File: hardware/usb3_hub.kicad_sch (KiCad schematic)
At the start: 39 parts, among them J7 USB3_B, J9 USB3_A, U8 USB7206C-I/KDX

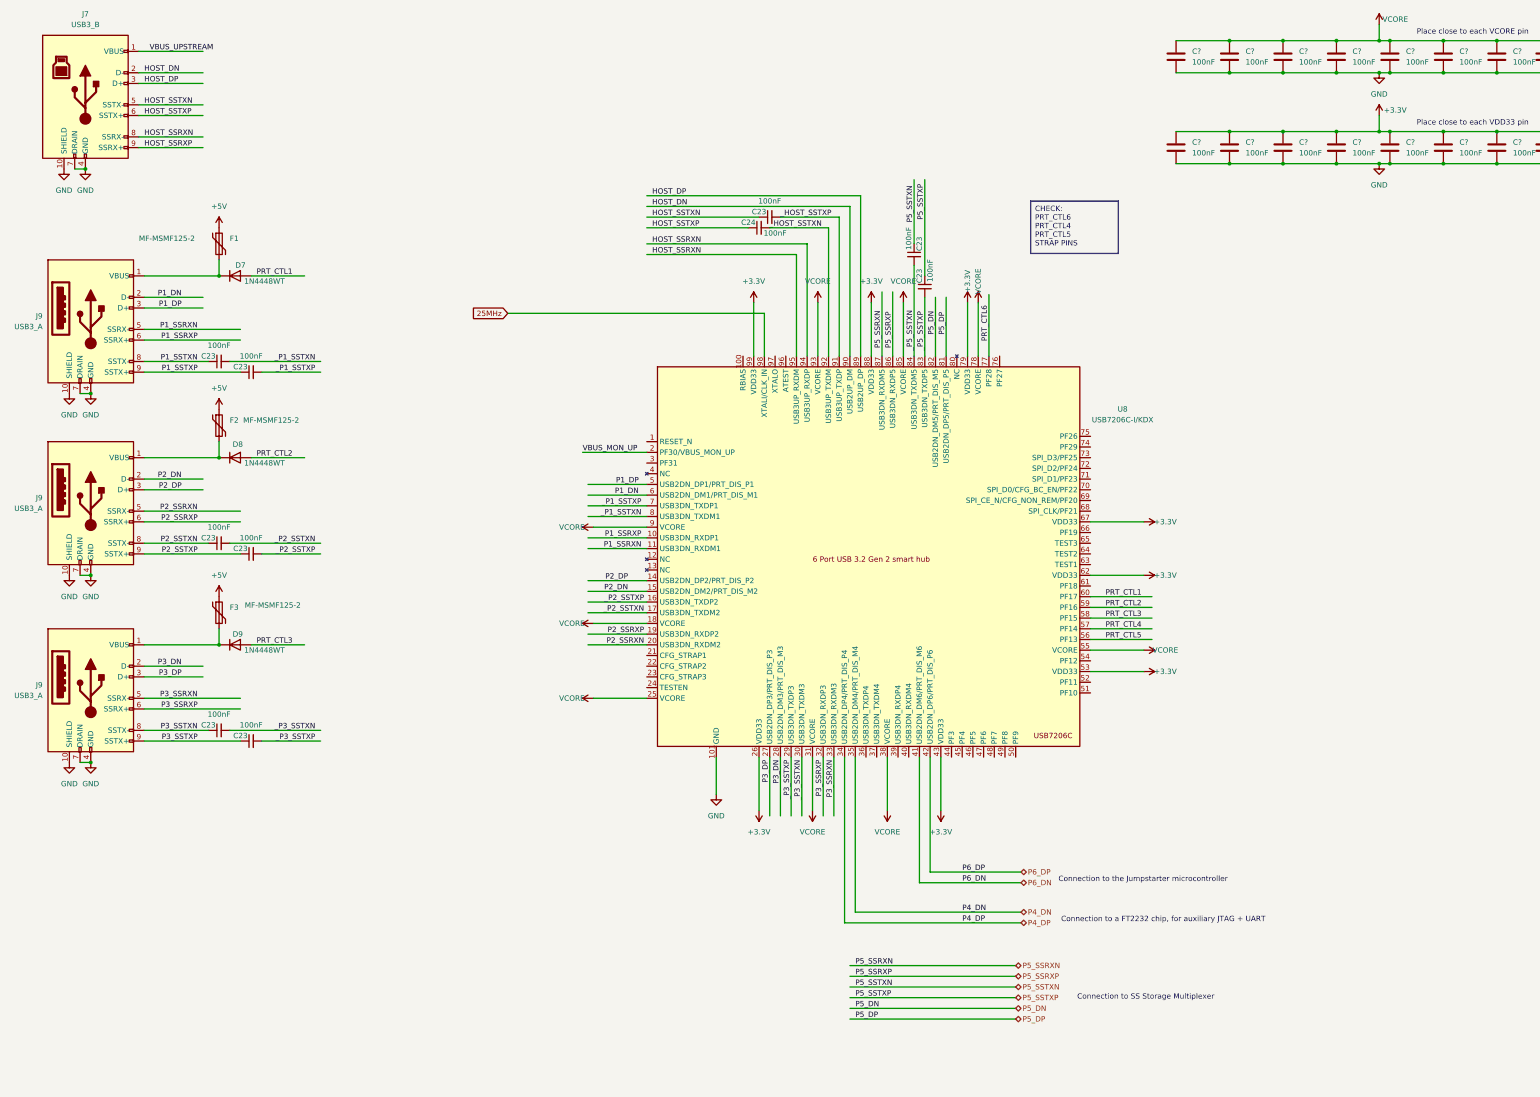
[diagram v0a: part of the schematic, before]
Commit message: Started routing USB3 diff pairs
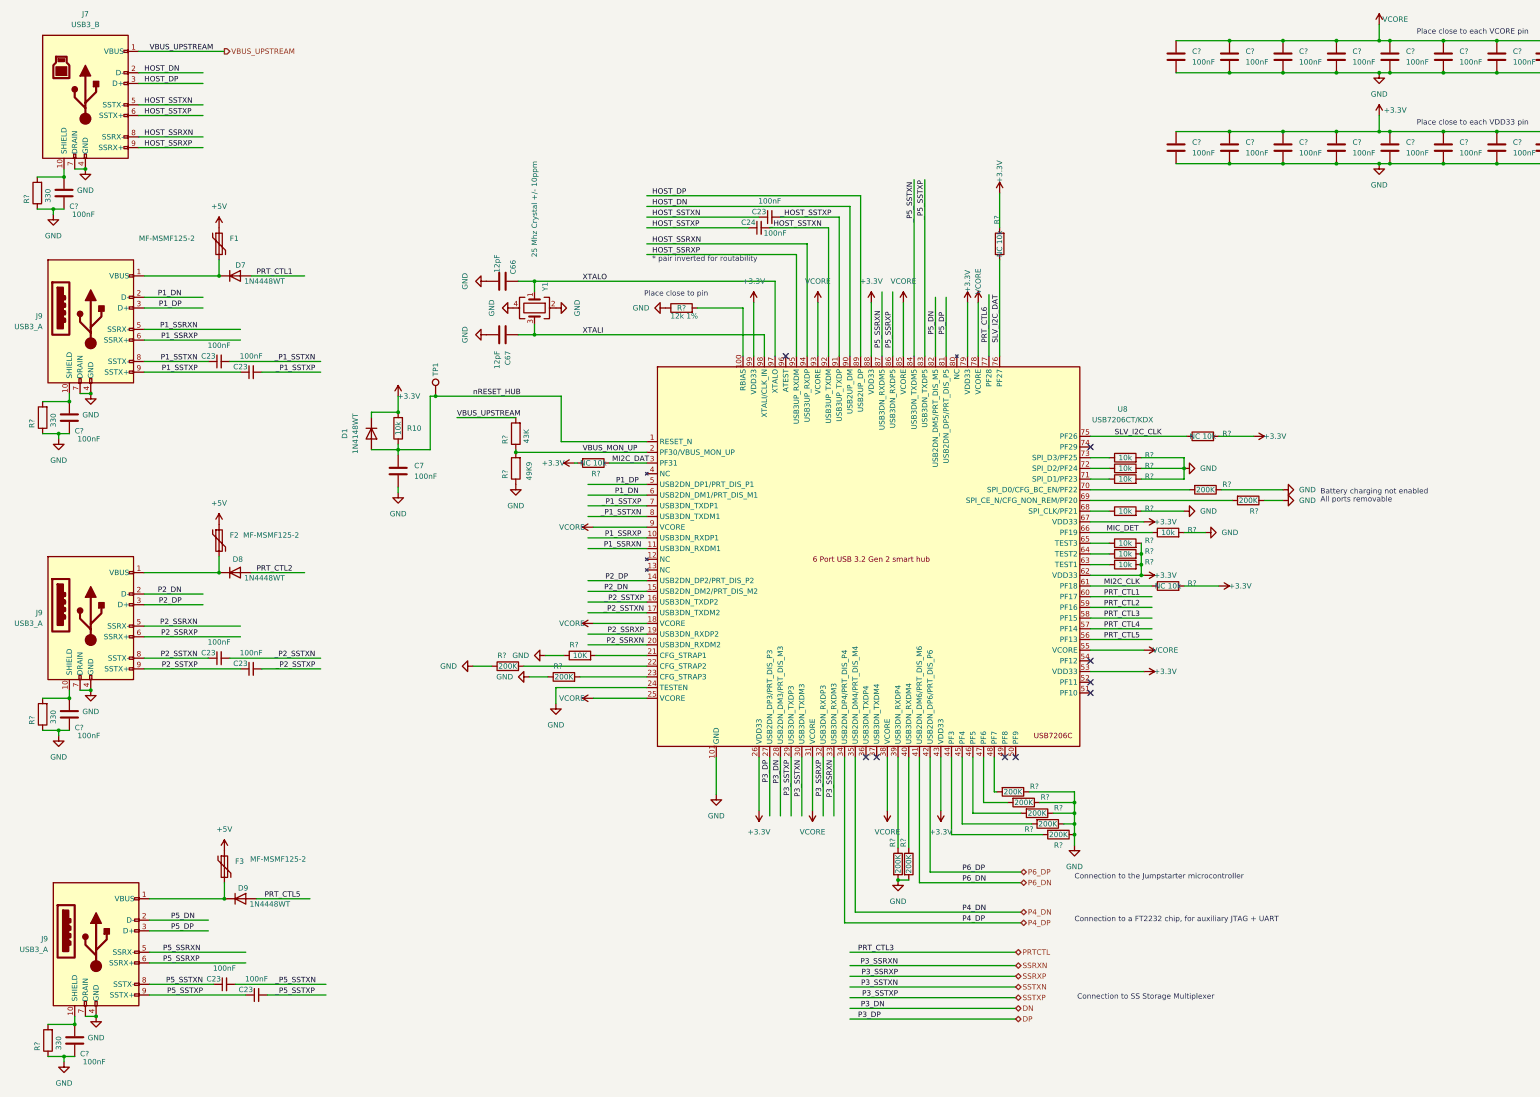
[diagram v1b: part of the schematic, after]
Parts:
- removed C23 (x2): 100nF, Capacitor_SMD:C_0402_1005Metric, symbol Device:C_Small
- added C66, C67: 12pF, Capacitor_SMD:C_0402_1005Metric, symbol Device:C
- added C7, C? (x4): 100nF, Capacitor_SMD:C_0402_1005Metric, symbol Device:C
- added D1: 1N4148WT, Diode_SMD:D_SOD-523, symbol Diode:1N4148WT
- added R10, R? (x8): 10k, Resistor_SMD:R_0402_1005Metric, symbol Device:R
- added R? (x11): 200K, Resistor_SMD:R_0402_1005Metric, symbol Device:R
- added R?: 49K9, Resistor_SMD:R_0402_1005Metric, symbol Device:R
- added R? (x4): 330, Resistor_SMD:R_0402_1005Metric, symbol Device:R
- added R? (x4): NC 10k, Resistor_SMD:R_0402_1005Metric, symbol Device:R
- added R?: 43K, Resistor_SMD:R_0402_1005Metric, symbol Device:R
- added R?: 12k 1%, Resistor_SMD:R_0402_1005Metric, symbol Device:R
- added R?: 10K, Resistor_SMD:R_0402_1005Metric, symbol Device:R
- added TP1: TestPoint, TestPoint:TestPoint_Pad_D1.0mm, symbol Connector:TestPoint
- added Y1: 25 Mhz Crystal +/- 10ppm, Oscillator:Oscillator_SMD_EuroQuartz_XO32-4Pin_3.2x2.5mm, symbol Device:Crystal_GND24
- C23, C24, C? (x18): MPN (none) -> CL05B104K05NNNC; MPN2 (none) -> TCC0402X7R104M160AT
- D7: MPN (none) -> 1N4448WT
- J9: footprint Connector_USB:USB3_A_Molex_48393-001 -> Connector_USB:SS-52000-004
- J9: footprint Connector_USB:USB3_A_Molex_48393-001 -> Connector_USB:SS-52000-004; Link (none) -> https://eu.mouser.com/ProductDetail/Stewart-Connector-Bel/S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; MFR Part (none) -> SS-52000-004
- U8: value USB7206C-I/KDX -> USB7206CT/KDX; Link (none) -> https://www.mouser.es/ProductDetail/Microchip-Technology/US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; MPN (none) -> USB7206CT/KDX
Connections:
- net P3_SSTXN is gone; now on net P5_SSTXN: C23.1, J9.8 (SSTX-)
- net P3_SSTXP is gone; now on net P5_SSTXP: C23.1, J9.9 (SSTX+)
- net +3.3V: now also D1.1 (K), R10.2, R?.2, R?.2, R?.2, R?.2, R?.2, R?.2, R?.2
- net GND: now also U8.24 (TESTEN), C66.1, C67.1, C7.1, C?.2, C?.2, C?.2, C?.2, R?.1, R?.1, R?.1, R?.1, R?.1, R?.1, R?.1, R?.1, R?.1, R?.1, R?.1, R?.1, R?.1, R?.1, R?.1, R?.1, R?.2, R?.2, R?.2, R?.2, R?.2, R?.2, R?.2, Y1.2, Y1.4; no longer J7.10 (SHIELD), J9.10 (SHIELD), J9.10 (SHIELD), J9.10 (SHIELD)
- net HOST_SSRXN: no longer U8.95 (USB3UP_RXDM)
- net HOST_SSRXP: now also U8.95 (USB3UP_RXDM)
- net P5_DN: now also J9.2 (D-)
- net P5_DP: now also J9.3 (D+)
- net P5_SSRXN: now also J9.5 (SSRX-)
- net P5_SSRXP: now also J9.6 (SSRX+)
- net PRT_CTL5: now also D9.2 (A)
- net VBUS_MON_UP: now also R?.1, R?.2
- net VBUS_UPSTREAM: now also R?.2
- net _P5_SSTXN: now also C23.2
- net _P5_SSTXP: now also C23.2
- net nRESET_HUB: now reaches U8.1 (RESET_N)
- net nRESET_HUB: now also C7.2, D1.2 (A), R10.1, TP1.1
- net at U8.100 (RBIAS): now also R?.2
- net at U8.21 (CFG_STRAP1): now also R?.2
- net at U8.22 (CFG_STRAP2): now also R?.2
- net at U8.23 (CFG_STRAP3): now also R?.2
- net MI2C_DAT: now reaches U8.3 (PF31)
- net MI2C_DAT: now also R?.1
- net at U8.39 (USB3DN_RXDP4): now also R?.1
- net at U8.40 (USB3DN_RXDM4): now also R?.1
- net at U8.44 (PF3): now also R?.2
- net at U8.45 (PF4): now also R?.2
- net at U8.46 (PF5): now also R?.2
- net at U8.47 (PF6): now also R?.2
- net at U8.48 (PF7): now also R?.2
- net MI2C_CLK: now reaches U8.61 (PF18)
- net MI2C_CLK: now also R?.1
- net at U8.63 (TEST1): now also R?.1
- net at U8.64 (TEST2): now also R?.1
- net at U8.65 (TEST3): now also R?.1
- net MIC_DET: now reaches U8.66 (PF19)
- net MIC_DET: now also R?.1
- net at U8.68 (SPI_CLK/PF21): now also R?.1
- net at U8.69 (SPI_CE_N/CFG_NON_REM/PF20): now also R?.2
- net at U8.70 (SPI_D0/CFG_BC_EN/PF22): now also R?.2
- net at U8.71 (SPI_D1/PF23): now also R?.1
- net at U8.72 (SPI_D2/PF24): now also R?.1
- net at U8.73 (SPI_D3/PF25): now also R?.1
- net SLV_I2C_CLK: now reaches U8.75 (PF26)
- net SLV_I2C_CLK: now also R?.1
- net SLV_I2C_DAT: now reaches U8.76 (PF27)
- net SLV_I2C_DAT: now also R?.1
- net XTALO: now reaches U8.97 (XTALO)
- net XTALO: now also C66.2, Y1.1
- net 25MHz renamed XTALI
- net XTALI: now also C67.2, Y1.3
- net P3_DN renamed DN
- net DN: no longer J9.2 (D-)
- net P3_DP renamed DP
- net DP: no longer J9.3 (D+)
- net P3_SSRXN renamed SSRXN
- net SSRXN: no longer J9.5 (SSRX-)
- net P3_SSRXP renamed SSRXP
- net SSRXP: no longer J9.6 (SSRX+)
- net PRT_CTL3 renamed PRTCTL
- net PRTCTL: no longer D9.2 (A)
- net _P3_SSTXN renamed SSTXN
- net SSTXN: no longer C23.2
- net _P3_SSTXP renamed SSTXP
- net SSTXP: no longer C23.2
- new net: C?.1, J9.10 (SHIELD), R?.2 (x3)
- new net: C?.1, J7.10 (SHIELD), R?.2
- no-connect marks 0 -> 9
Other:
- note added: "* pair inverted for routability"
- note added: "All ports removable"
- note added: "Battery charging not enabled"
- note added: "Place close to pin"
- moved on the sheet: C23, D8, D9, F2, F3, J9

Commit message: Routing and several design fixes
Signed-off-by: Miguel Angel Ajo Pelayo <majopela@redhat.com>
Signed-off-by: Ricardo Noriega <rnoriega@redhat.com>
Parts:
- R? (x3): value NC 10k -> 10k; fit_field dnp -> (none)
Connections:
- net +3.3V: no longer R?.2, R?.2, R?.2
- net GND: now also R?.2, R?.2, R?.2
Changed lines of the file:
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@@
     )
   )
-  (symbol (lib_id "power:+3.3V") (at 307.975 116.84 270) (unit 1)
-    (in_bom yes) (on_board yes) (dnp no)
-    (property "Reference" "#PWR013" (at 304.165 116.84 0)
+  (symbol (lib_id "power:GND") (at 307.975 116.84 90) (unit 1)
+    (in_bom yes) (on_board yes) (dnp no) (fields_autoplaced)
+    (property "Reference" "#PWR?" (at 314.325 116.84 0)
       (effects (font (size 1.27 1.27)) hide)
     )
-    (property "Value" "+3.3V" (at 313.055 116.84 90)
-      (effects (font (size 1.27 1.27)))
+    (property "Value" "GND" (at 311.785 116.84 90)
+      (effects (font (size 1.27 1.27)) (justify right))
     )
     (property "Footprint" "" (at 307.975 116.84 0)
@@
       (project "jumpstarter"
         (path "/5e49fb74-0a9b-4946-8b59-2b8244d10fd9"
-          (reference "#PWR013") (unit 1)
+          (reference "#PWR?") (unit 1)
+        )
+        (path "/5e49fb74-0a9b-4946-8b59-2b8244d10fd9/0a246f5a-dd08-4f47-947a-3b89ae06d789"
+          (reference "#PWR03") (unit 1)
         )
         (path "/5e49fb74-0a9b-4946-8b59-2b8244d10fd9/c1addf8b-26b2-43fb-875c-11d76afd1403"
@@
       (effects (font (size 1.27 1.27)))
     )
-    (property "Value" "NC 10k" (at 287.655 152.4 90)
+    (property "Value" "10k" (at 287.655 152.4 90)
       (effects (font (size 1.27 1.27)))
     )
@@
       (effects (font (size 1.27 1.27)) hide)
     )
-    (property "fit_field" "dnp" (at 287.655 152.4 90)
-      (effects (font (size 1.27 1.27)) hide)
-    )
     (pin "1")
     (pin "2")
@@
     )
   )
+  (symbol (lib_id "power:GND") (at 299.72 152.4 90) (unit 1)
+    (in_bom yes) (on_board yes) (dnp no) (fields_autoplaced)
+    (property "Reference" "#PWR?" (at 306.07 152.4 0)
+      (effects (font (size 1.27 1.27)) hide)
+    )
+    (property "Value" "GND" (at 303.53 152.4 90)
+      (effects (font (size 1.27 1.27)) (justify right))
+    )
+    (property "Footprint" "" (at 299.72 152.4 0)
+      (effects (font (size 1.27 1.27)) hide)
+    )
+    (property "Datasheet" "" (at 299.72 152.4 0)
+      (effects (font (size 1.27 1.27)) hide)
+    )
+    (pin "1")
+    (instances
+      (project "jumpstarter"
+        (path "/5e49fb74-0a9b-4946-8b59-2b8244d10fd9"
+          (reference "#PWR?") (unit 1)
+        )
+        (path "/5e49fb74-0a9b-4946-8b59-2b8244d10fd9/0a246f5a-dd08-4f47-947a-3b89ae06d789"
+          (reference "#PWR03") (unit 1)
+        )
+        (path "/5e49fb74-0a9b-4946-8b59-2b8244d10fd9/c1addf8b-26b2-43fb-875c-11d76afd1403"
+          (reference "#PWR083") (unit 1)
+        )
+      )
+    )
+  )
   (symbol (lib_id "power:+3.3V") (at 190.5 205.74 180) (unit 1)
     (in_bom yes) (on_board yes) (dnp no)
@@
     )
   )
-  (symbol (lib_id "power:+3.3V") (at 247.65 59.055 0) (unit 1)
-    (in_bom yes) (on_board yes) (dnp no)
-    (property "Reference" "#PWR013" (at 247.65 62.865 0)
-      (effects (font (size 1.27 1.27)) hide)
-    )
-    (property "Value" "+3.3V" (at 247.65 53.975 90)
-      (effects (font (size 1.27 1.27)))
-    )
-    (property "Footprint" "" (at 247.65 59.055 0)
-      (effects (font (size 1.27 1.27)) hide)
-    )
-    (property "Datasheet" "" (at 247.65 59.055 0)
-      (effects (font (size 1.27 1.27)) hide)
-    )
-    (pin "1")
-    (instances
-      (project "jumpstarter"
-        (path "/5e49fb74-0a9b-4946-8b59-2b8244d10fd9"
-          (reference "#PWR013") (unit 1)
-        )
-        (path "/5e49fb74-0a9b-4946-8b59-2b8244d10fd9/c1addf8b-26b2-43fb-875c-11d76afd1403"
-          (reference "#PWR0220") (unit 1)
-        )
-      )
-    )
-  )
   (symbol (lib_id "POWER:VCORE") (at 151.13 138.43 90) (unit 1)
     (in_bom yes) (on_board yes) (dnp no)
@@
     )
   )
+  (symbol (lib_id "power:GND") (at 247.65 59.055 180) (unit 1)
+    (in_bom yes) (on_board yes) (dnp no) (fields_autoplaced)
+    (property "Reference" "#PWR?" (at 247.65 52.705 0)
+      (effects (font (size 1.27 1.27)) hide)
+    )
+    (property "Value" "GND" (at 247.65 54.61 0)
+      (effects (font (size 1.27 1.27)))
+    )
+    (property "Footprint" "" (at 247.65 59.055 0)
+      (effects (font (size 1.27 1.27)) hide)
+    )
+    (property "Datasheet" "" (at 247.65 59.055 0)
+      (effects (font (size 1.27 1.27)) hide)
+    )
+    (pin "1")
+    (instances
+      (project "jumpstarter"
+        (path "/5e49fb74-0a9b-4946-8b59-2b8244d10fd9"
+          (reference "#PWR?") (unit 1)
+        )
+        (path "/5e49fb74-0a9b-4946-8b59-2b8244d10fd9/0a246f5a-dd08-4f47-947a-3b89ae06d789"
+          (reference "#PWR03") (unit 1)
+        )
+        (path "/5e49fb74-0a9b-4946-8b59-2b8244d10fd9/c1addf8b-26b2-43fb-875c-11d76afd1403"
+          (reference "#PWR0220") (unit 1)
+        )
+      )
+    )
+  )
   (symbol (lib_id "Device:C") (at 129.54 80.01 90) (unit 1)
     (in_bom yes) (on_board yes) (dnp no)
@@
       (effects (font (size 1.27 1.27)))
     )
-    (property "Value" "NC 10k" (at 295.91 116.84 90)
+    (property "Value" "10k" (at 295.91 116.84 90)
       (effects (font (size 1.27 1.27)))
     )
@@
       (effects (font (size 1.27 1.27)) hide)
     )
-    (property "fit_field" "dnp" (at 295.91 116.84 90)
-      (effects (font (size 1.27 1.27)) hide)
-    )
     (pin "1")
     (pin "2")
@@
     )
   )
-  (symbol (lib_id "power:+3.3V") (at 299.72 152.4 270) (unit 1)
-    (in_bom yes) (on_board yes) (dnp no)
-    (property "Reference" "#PWR013" (at 295.91 152.4 0)
-      (effects (font (size 1.27 1.27)) hide)
-    )
-    (property "Value" "+3.3V" (at 304.8 152.4 90)
-      (effects (font (size 1.27 1.27)))
-    )
-    (property "Footprint" "" (at 299.72 152.4 0)
-      (effects (font (size 1.27 1.27)) hide)
-    )
-    (property "Datasheet" "" (at 299.72 152.4 0)
-      (effects (font (size 1.27 1.27)) hide)
-    )
-    (pin "1")
-    (instances
-      (project "jumpstarter"
-        (path "/5e49fb74-0a9b-4946-8b59-2b8244d10fd9"
-          (reference "#PWR013") (unit 1)
-        )
-        (path "/5e49fb74-0a9b-4946-8b59-2b8244d10fd9/c1addf8b-26b2-43fb-875c-11d76afd1403"
-          (reference "#PWR0223") (unit 1)
-        )
-      )
-    )
-  )
   (symbol (lib_id "Device:C") (at 289.56 26.67 0) (unit 1)
     (in_bom yes) (on_board yes) (dnp no)
@@
       (effects (font (size 1.27 1.27)))
     )
-    (property "Value" "NC 10k" (at 247.65 71.12 90)
+    (property "Value" "10k" (at 247.65 71.12 90)
       (effects (font (size 1.27 1.27)))
     )
@@
       (effects (font (size 1.27 1.27)) hide)
     )
-    (property "fit_field" "dnp" (at 247.65 71.12 90)
-      (effects (font (size 1.27 1.27)) hide)
-    )

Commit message: Almost ready 2.0.0
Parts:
- C23, C24, C7, C? (x22): MFN (none) -> CL10B104KB8NNNC
- C66, C67: MFN (none) -> CC0402JRNPO9BN120; MPN (none) -> CC0402JRNPO9BN120
- D1: Link (none) -> https://eu.mouser.com/ProductDetail/onsemi-Fairchild/1N4148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; MFN (none) -> 1N4148WT; MPN (none) -> 1N4148WT
- D7: Link (none) -> https://www2.mouser.com/ProductDetail/onsemi-Fairchild/1N44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; MFN (none) -> 1N4448WT
- D8, D9: Link (none) -> https://www2.mouser.com/ProductDetail/onsemi-Fairchild/1N44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; MFN (none) -> 1N4448WT; MPN (none) -> 1N4448WT
- F1, F2, F3: MFN (none) -> MF-MSMF125-2; MPN (none) -> MF-MSMF125-2
- J7: Link (none) -> https://es.farnell.com/wurth-elektronik/692221030100/usb-3-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; MFN (none) -> 692221030100; MPN (none) -> 692221030100
- J9: Link (none) -> https://eu.mouser.com/ProductDetail/Stewart-Connector-Bel/S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; MFN (none) -> SS-52000-004; MFR Part (none) -> SS-52000-004; MPN (none) -> SS-52000-004
- J9: MFN (none) -> SS-52000-004; MPN (none) -> SS-52000-004
- R10, R? (x11): MFN (none) -> RTT02103JTH; MPN (none) -> RTT02103JTH
- R? (x11): MFN (none) -> RTT02204JTH; MPN (none) -> RTT02204JTH
- R?: value 49K9 -> 49K9 1%; MFN (none) -> RTT024992FTH; MPN (none) -> RTT024992FTH
- R? (x4): MFN (none) -> RTT02331JTH; MPN (none) -> RTT02331JTH
- R?: MFN (none) -> NC; MPN (none) -> NC
- R?: MFN (none) -> CR0402FF4302G; MPN (none) -> CR0402FF4302G
- R?: MFN (none) -> RTT021202FTH; MPN (none) -> RTT021202FTH
- R?: value 10K -> 10k; MFN (none) -> RTT02103JTH; MPN (none) -> RTT02103JTH
- U8: MFN (none) -> USB7206CT/KDX
- Y1: MFN (none) -> SX32Y025000BG1T
